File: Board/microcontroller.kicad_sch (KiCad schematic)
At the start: 32 parts, among them J10 FAN, J11 DUO LED, J9 ICSP, Q7 IRLML2502, SW1 CALIBRATE, U2 PIC18F2480-ISO, Y1 10 MHz

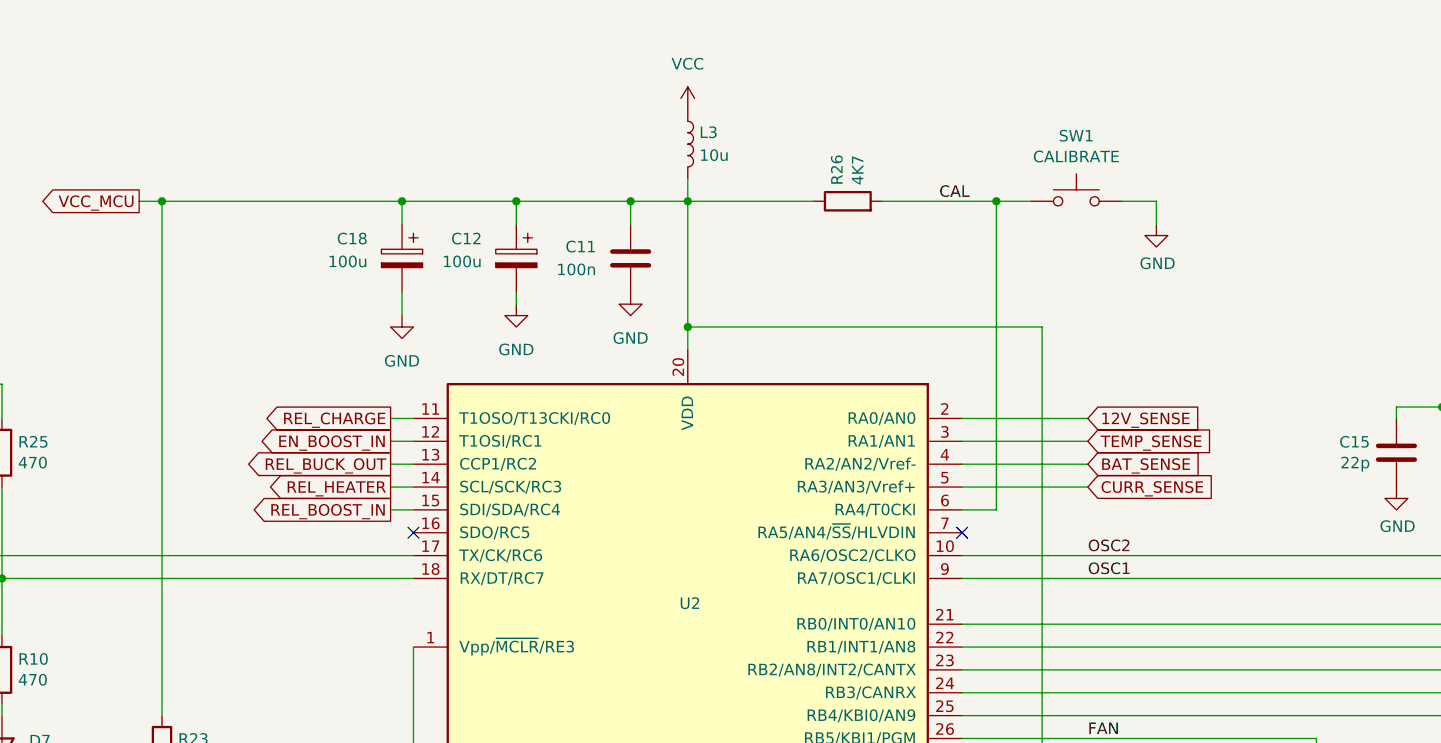
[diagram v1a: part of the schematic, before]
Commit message: - REL_HEATER is now RA5 (was RC3) - REL_BOOST_IN is now RC5 (was RC4) Add I2C OLED display connector Add AGENTS.md
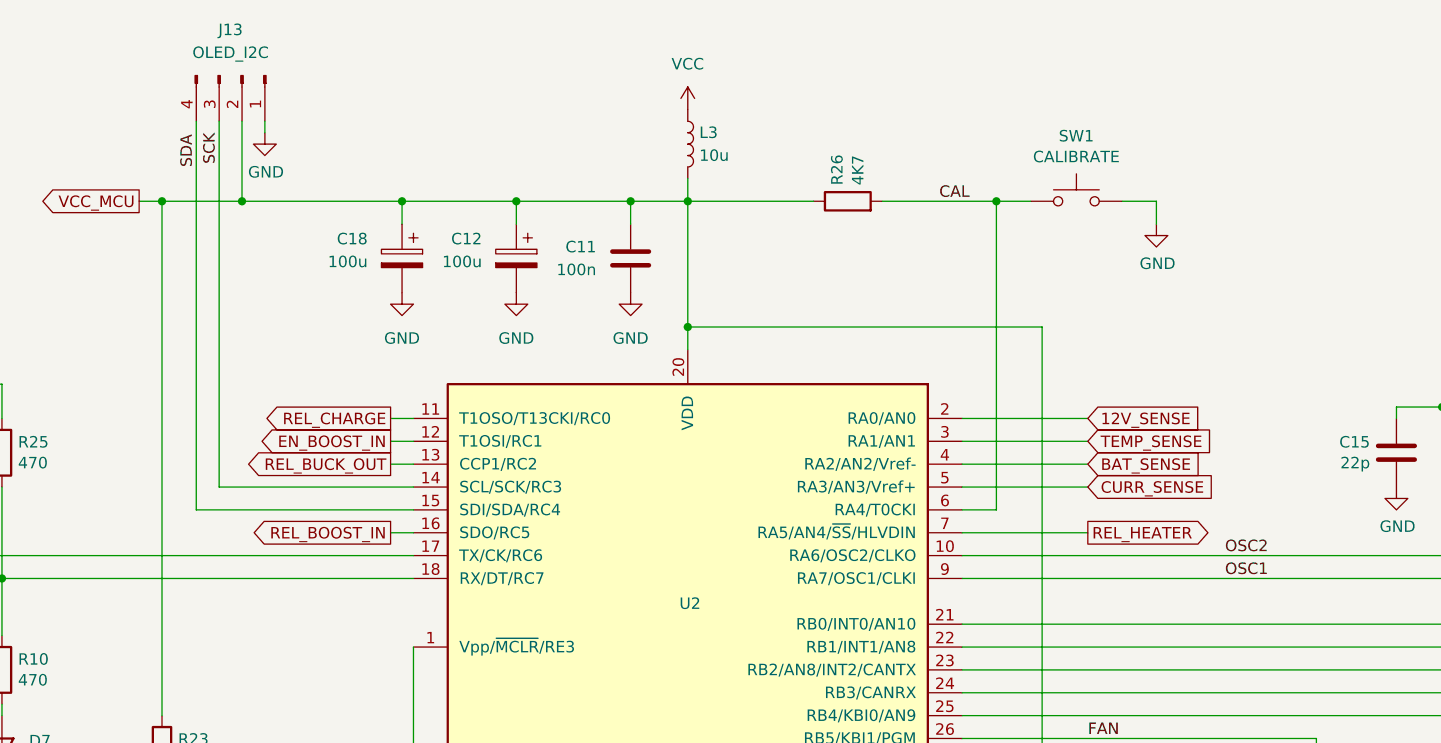
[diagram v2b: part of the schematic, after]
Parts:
- added J13: OLED_I2C, Connector_JST:JST_PH_B4B-PH-K_1x04_P2.00mm_Vertical, symbol Connector:Conn_01x04_Pin
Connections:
- net GND: now also J13.1 (Pin_1)
- net REL_BOOST_IN: now also U2.16 (SDO/RC5); no longer U2.15 (SDI/SDA/RC4)
- net REL_HEATER: now also U2.7 (RA5/AN4/~{SS}/HLVDIN); no longer U2.14 (SCL/SCK/RC3)
- net VCC_MCU: now also J13.2 (Pin_2)
- new net SCK: J13.3 (Pin_3), U2.14 (SCL/SCK/RC3)
- new net SDA: J13.4 (Pin_4), U2.15 (SDI/SDA/RC4)
- no-connect marks 2 -> 0
